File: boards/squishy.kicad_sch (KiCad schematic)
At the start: 56 parts, among them J1 USB_B_Micro, J2 Conn_02x26_Top_Bottom, J3 Conn_01x04, J4 Conn_02x05_Odd_Even, Q1 Q_PMOS_DGS, U12 SP3400-02UTG, U14 USB3318, U19 ICE40HX8K-BG121, U26 W25N01GVZEIG, X1 16MHz, X2 48MHz

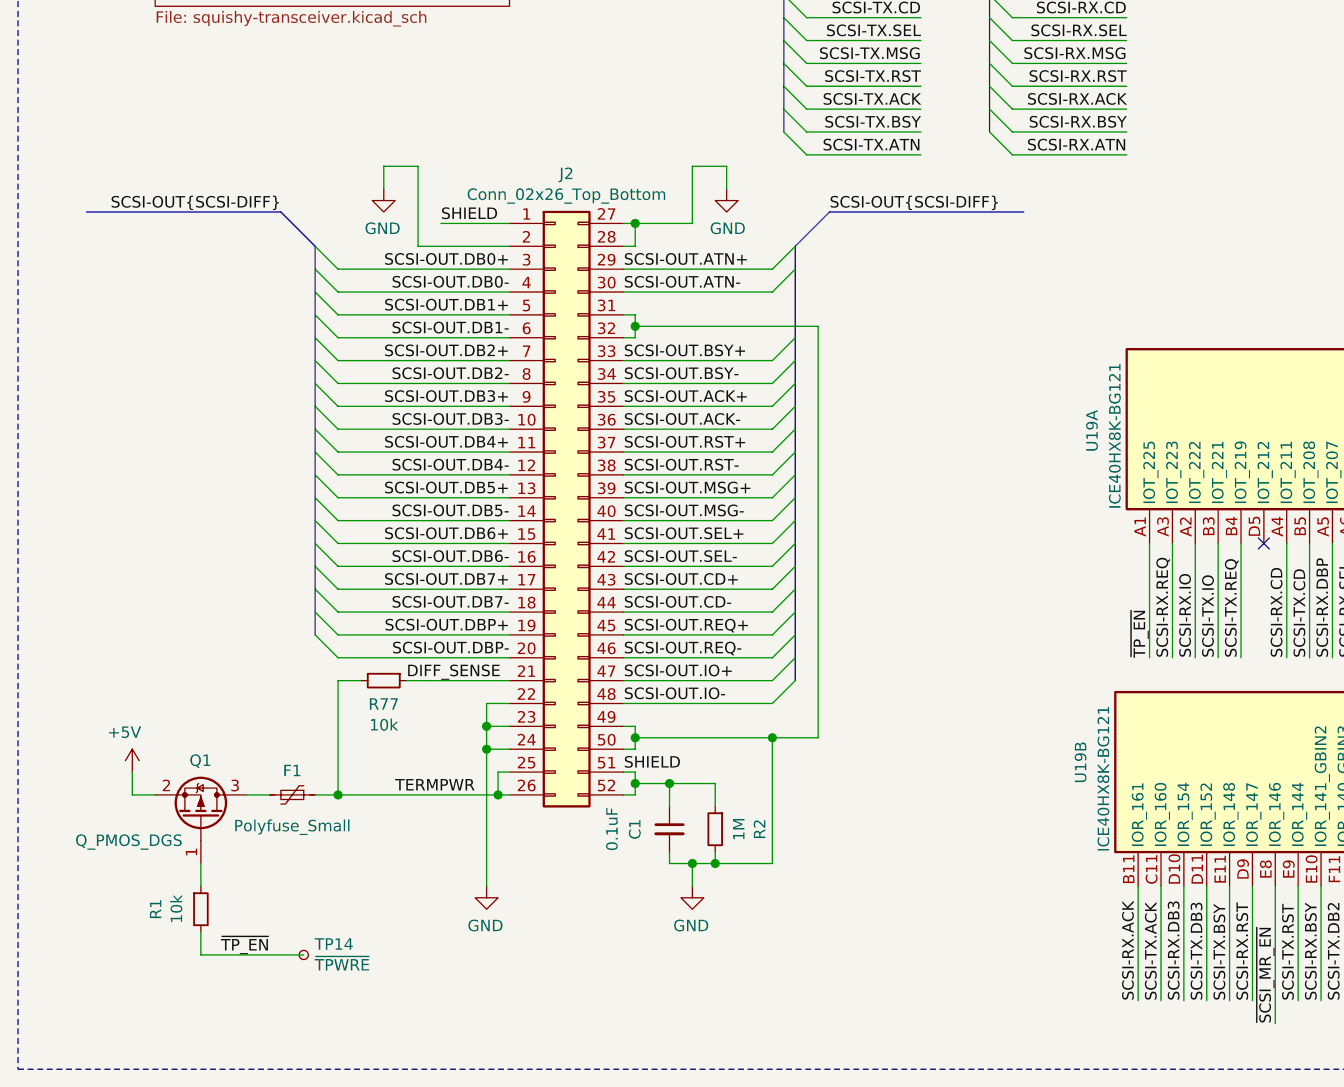
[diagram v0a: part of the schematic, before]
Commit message: hardware: found an error with how the SCSI connector was laid out, fixed that, oh no, my poor pcb
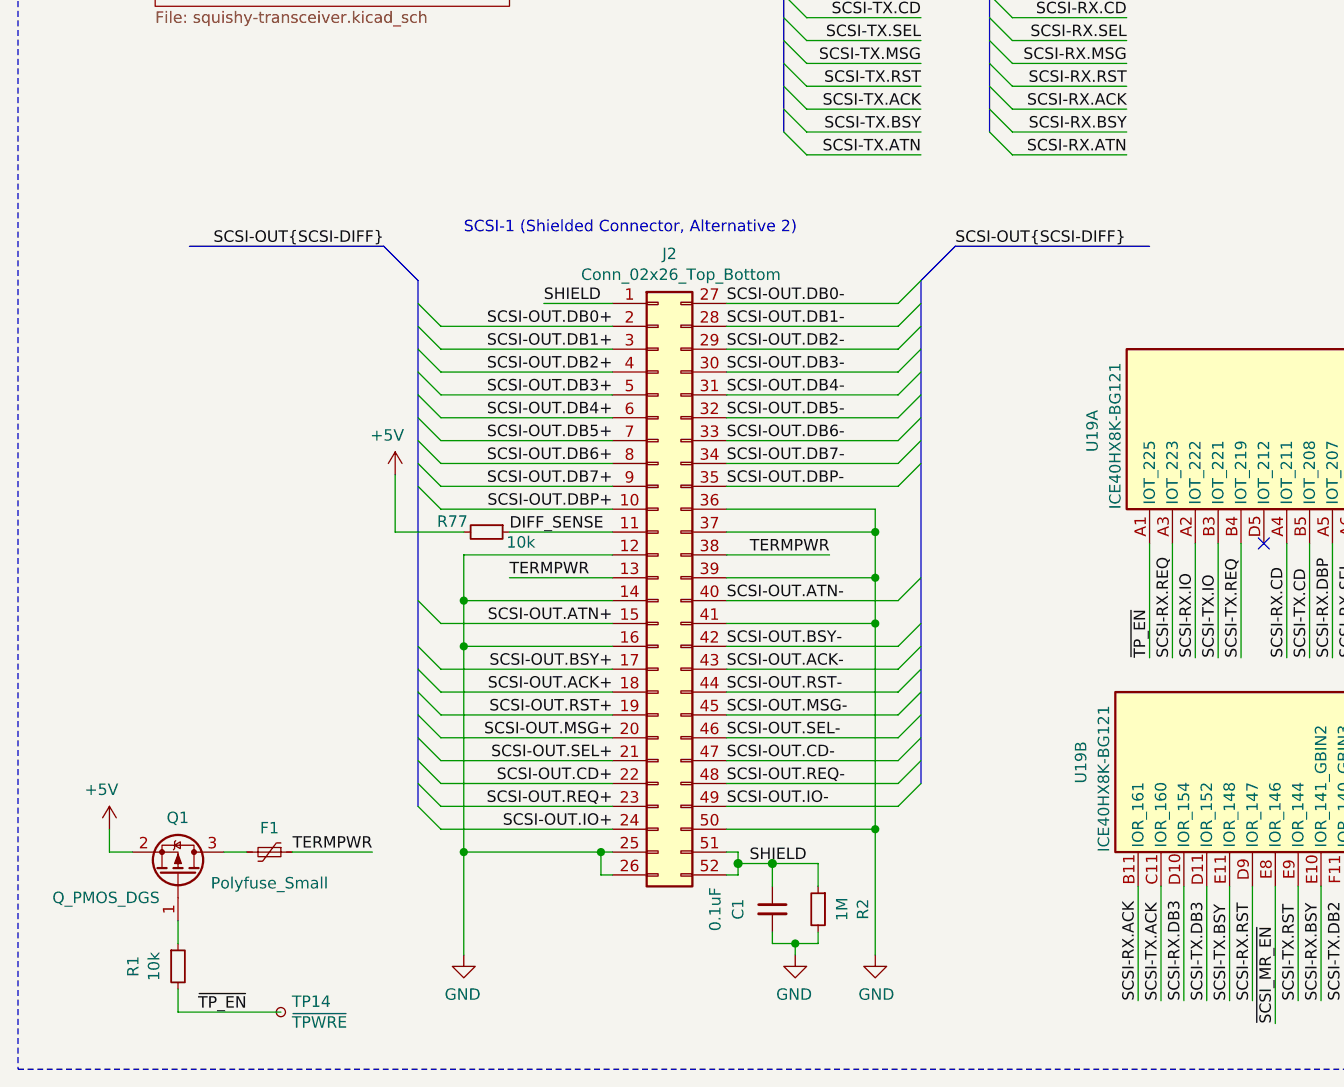
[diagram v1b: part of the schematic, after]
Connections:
- net +5V: now also R77.2
- net DIFF_SENSE: now also J2.11 (Pin_11); no longer J2.21 (Pin_21)
- net GND: now also J2.12 (Pin_12), J2.14 (Pin_14), J2.16 (Pin_16), J2.25 (Pin_25), J2.26 (Pin_26), J2.36 (Pin_36), J2.37 (Pin_37), J2.39 (Pin_39), J2.41 (Pin_41); no longer J2.2 (Pin_2), J2.22 (Pin_22), J2.23 (Pin_23), J2.24 (Pin_24), J2.27 (Pin_27), J2.28 (Pin_28), J2.31 (Pin_31), J2.32 (Pin_32), J2.49 (Pin_49)
- net SCSI-OUT.ACK+: now also J2.18 (Pin_18); no longer J2.35 (Pin_35)
- net SCSI-OUT.ACK-: now also J2.43 (Pin_43); no longer J2.36 (Pin_36)
- net SCSI-OUT.ATN+: now also J2.15 (Pin_15); no longer J2.29 (Pin_29)
- net SCSI-OUT.ATN-: now also J2.40 (Pin_40); no longer J2.30 (Pin_30)
- net SCSI-OUT.BSY+: now also J2.17 (Pin_17); no longer J2.33 (Pin_33)
- net SCSI-OUT.BSY-: now also J2.42 (Pin_42); no longer J2.34 (Pin_34)
- net SCSI-OUT.CD+: now also J2.22 (Pin_22); no longer J2.43 (Pin_43)
- net SCSI-OUT.CD-: now also J2.47 (Pin_47); no longer J2.44 (Pin_44)
- net SCSI-OUT.DB0+: now also J2.2 (Pin_2); no longer J2.3 (Pin_3)
- net SCSI-OUT.DB0-: now also J2.27 (Pin_27); no longer J2.4 (Pin_4)
- net SCSI-OUT.DB1+: now also J2.3 (Pin_3); no longer J2.5 (Pin_5)
- net SCSI-OUT.DB1-: now also J2.28 (Pin_28); no longer J2.6 (Pin_6)
- net SCSI-OUT.DB2+: now also J2.4 (Pin_4); no longer J2.7 (Pin_7)
- net SCSI-OUT.DB2-: now also J2.29 (Pin_29); no longer J2.8 (Pin_8)
- net SCSI-OUT.DB3+: now also J2.5 (Pin_5); no longer J2.9 (Pin_9)
- net SCSI-OUT.DB3-: now also J2.30 (Pin_30); no longer J2.10 (Pin_10)
- net SCSI-OUT.DB4+: now also J2.6 (Pin_6); no longer J2.11 (Pin_11)
- net SCSI-OUT.DB4-: now also J2.31 (Pin_31); no longer J2.12 (Pin_12)
- net SCSI-OUT.DB5+: now also J2.7 (Pin_7); no longer J2.13 (Pin_13)
- net SCSI-OUT.DB5-: now also J2.32 (Pin_32); no longer J2.14 (Pin_14)
- net SCSI-OUT.DB6+: now also J2.8 (Pin_8); no longer J2.15 (Pin_15)
- net SCSI-OUT.DB6-: now also J2.33 (Pin_33); no longer J2.16 (Pin_16)
- net SCSI-OUT.DB7+: now also J2.9 (Pin_9); no longer J2.17 (Pin_17)
- net SCSI-OUT.DB7-: now also J2.34 (Pin_34); no longer J2.18 (Pin_18)
- net SCSI-OUT.DBP+: now also J2.10 (Pin_10); no longer J2.19 (Pin_19)
- net SCSI-OUT.DBP-: now also J2.35 (Pin_35); no longer J2.20 (Pin_20)
- net SCSI-OUT.IO+: now also J2.24 (Pin_24); no longer J2.47 (Pin_47)
- net SCSI-OUT.IO-: now also J2.49 (Pin_49); no longer J2.48 (Pin_48)
- net SCSI-OUT.MSG+: now also J2.20 (Pin_20); no longer J2.39 (Pin_39)
- net SCSI-OUT.MSG-: now also J2.45 (Pin_45); no longer J2.40 (Pin_40)
- net SCSI-OUT.REQ+: now also J2.23 (Pin_23); no longer J2.45 (Pin_45)
- net SCSI-OUT.REQ-: now also J2.48 (Pin_48); no longer J2.46 (Pin_46)
- net SCSI-OUT.RST+: now also J2.19 (Pin_19); no longer J2.37 (Pin_37)
- net SCSI-OUT.RST-: now also J2.44 (Pin_44); no longer J2.38 (Pin_38)
- net SCSI-OUT.SEL+: now also J2.21 (Pin_21); no longer J2.41 (Pin_41)
- net SCSI-OUT.SEL-: now also J2.46 (Pin_46); no longer J2.42 (Pin_42)
- net TERMPWR: now also J2.13 (Pin_13), J2.38 (Pin_38); no longer J2.25 (Pin_25), J2.26 (Pin_26), R77.2
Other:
- note added: "SCSI-1 (Shielded Connector, Alternative 2)"
- moved on the sheet: C1, F1, J2, Q1, R1, R2, R77, TP14

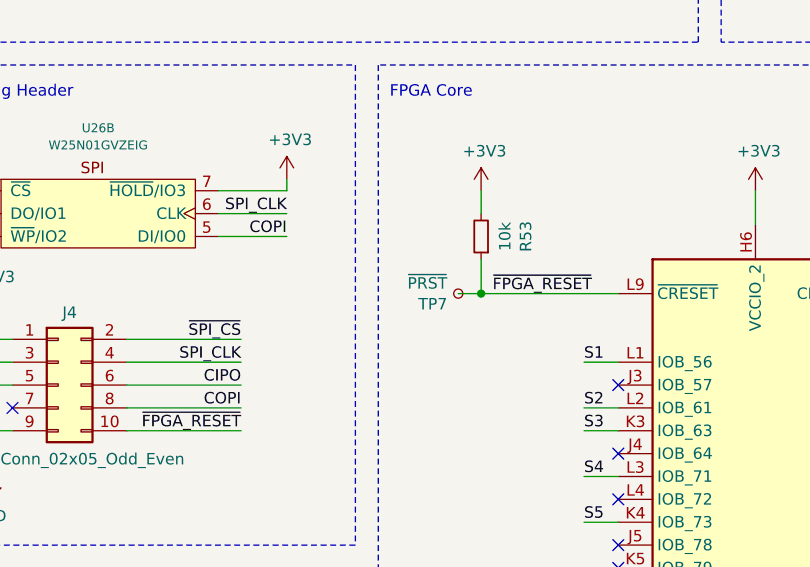
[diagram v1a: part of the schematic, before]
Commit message: hardware: ensured all of the parts had a mpn and mfr
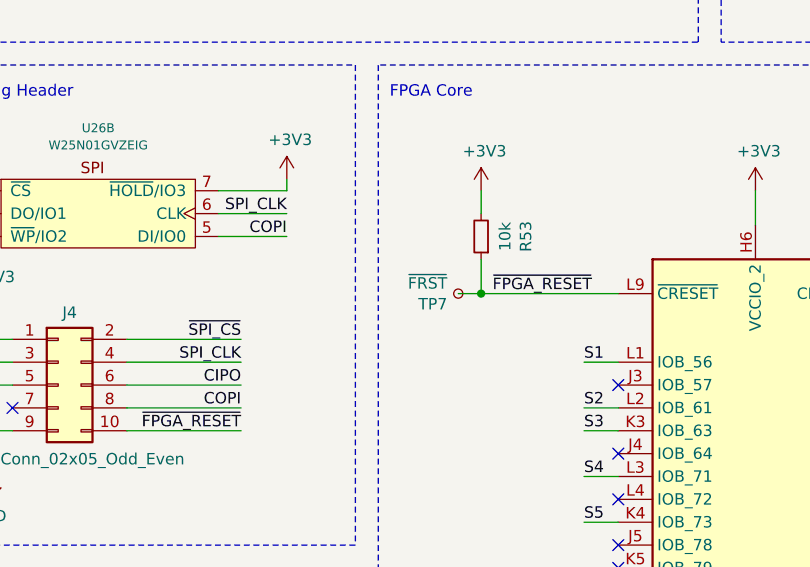
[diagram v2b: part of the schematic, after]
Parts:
- C30, C48: MFR KEMET -> Murata Electronics; MPN (none) -> GRJ21BR61E106KE01K
- C60: MFR (none) -> Taiyo Yuden; MPN (none) -> UMK107BJ105KA-T
- R57, R62: MFR (none) -> TE Connectivity Passive Product; MPN (none) -> CRG0603F100R
- R72: MFR (none) -> Vishay Dale; MPN (none) -> CRCW06038K06FKEAC
- TP10, TP11, TP12, TP13, TP14, TP6, TP8, TP9: MFR (none) -> N/A; MPN (none) -> N/A
- TP7: value ~{PRST} -> ~{FRST}; MFR (none) -> N/A; MPN (none) -> N/A
- U19: MFR Lattice Semicondutors -> Lattice Semiconductors
- U19: MFR Lattice Semiconducrtors -> Lattice Semiconductors
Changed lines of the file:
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@@
       (effects (font (size 1.27 1.27)) hide)
     )
+    (property "MFR" "N/A" (id 4) (at 30.48 121.92 0)
+      (effects (font (size 1.27 1.27)) hide)
+    )
+    (property "MPN" "N/A" (id 5) (at 30.48 121.92 0)
+      (effects (font (size 1.27 1.27)) hide)
+    )
     (pin "1")
   )
@@
       (effects (font (size 1.27 1.27)) hide)
     )
+    (property "MFR" "N/A" (id 4) (at 43.18 276.86 0)
+      (effects (font (size 1.27 1.27)) hide)
+    )
+    (property "MPN" "N/A" (id 5) (at 43.18 276.86 0)
+      (effects (font (size 1.27 1.27)) hide)
+    )
     (pin "1")
   )
@@
       (effects (font (size 1.27 1.27)) hide)
     )
+    (property "MFR" "N/A" (id 4) (at 208.28 133.35 0)
+      (effects (font (size 1.27 1.27)) hide)
+    )
+    (property "MPN" "N/A" (id 5) (at 208.28 133.35 0)
+      (effects (font (size 1.27 1.27)) hide)
+    )
     (pin "1")
   )
@@
       (effects (font (size 1.27 1.27)) hide)
     )
+    (property "MFR" "N/A" (id 4) (at 208.28 138.43 0)
+      (effects (font (size 1.27 1.27)) hide)
+    )
+    (property "MPN" "N/A" (id 5) (at 208.28 138.43 0)
+      (effects (font (size 1.27 1.27)) hide)
+    )
     (pin "1")
   )
@@
       (effects (font (size 1.27 1.27)) hide)
     )
+    (property "MFR" "N/A" (id 4) (at 208.28 143.51 0)
+      (effects (font (size 1.27 1.27)) hide)
+    )
+    (property "MPN" "N/A" (id 5) (at 208.28 143.51 0)
+      (effects (font (size 1.27 1.27)) hide)
+    )
     (pin "1")
   )
@@
       (effects (font (size 1.27 1.27)) hide)
     )
+    (property "MFR" "N/A" (id 4) (at 208.28 148.59 0)
+      (effects (font (size 1.27 1.27)) hide)
+    )
+    (property "MPN" "N/A" (id 5) (at 208.28 148.59 0)
+      (effects (font (size 1.27 1.27)) hide)
+    )
     (pin "1")
   )
@@
       (effects (font (size 1.27 1.27)) hide)
     )
+    (property "MFR" "N/A" (id 4) (at 208.28 153.67 0)
+      (effects (font (size 1.27 1.27)) hide)
+    )
+    (property "MPN" "N/A" (id 5) (at 208.28 153.67 0)
+      (effects (font (size 1.27 1.27)) hide)
+    )
     (pin "1")
   )
@@
       (effects (font (size 1.27 1.27)) hide)
     )
+    (property "MFR" "N/A" (id 4) (at 208.28 158.75 0)
+      (effects (font (size 1.27 1.27)) hide)
+    )
+    (property "MPN" "N/A" (id 5) (at 208.28 158.75 0)
+      (effects (font (size 1.27 1.27)) hide)
+    )
     (pin "1")
   )
@@
       (effects (font (size 1.27 1.27)) (justify left))
     )
-    (property "Value" "~{PRST}" (id 1) (at 227.3808 96.647 0)
+    (property "Value" "~{FRST}" (id 1) (at 227.3808 96.647 0)
       (effects (font (size 1.27 1.27)) (justify left))
     )
@@
       (effects (font (size 1.27 1.27)) hide)
     )
+    (property "MFR" "N/A" (id 4) (at 228.6 97.79 0)
+      (effects (font (size 1.27 1.27)) hide)
+    )
+    (property "MPN" "N/A" (id 5) (at 228.6 97.79 0)
+      (effects (font (size 1.27 1.27)) hide)
+    )
     (pin "1")
   )
@@
       (effects (font (size 1.27 1.27)) hide)
     )
-    (property "MFR" "" (id 4) (at 123.19 35.56 90)
+    (property "MFR" "Vishay Dale" (id 4) (at 123.19 35.56 90)
       (effects (font (size 1.27 1.27)) hide)
     )
-    (property "MPN" "" (id 5) (at 123.19 35.56 90)
+    (property "MPN" "CRCW06038K06FKEAC" (id 5) (at 123.19 35.56 90)
       (effects (font (size 1.27 1.27)) hide)
     )
@@
       (effects (font (size 1.27 1.27)) hide)
     )
-    (property "MFR" "" (id 4) (at 331.47 101.6 90)
+    (property "MFR" "TE Connectivity Passive Product" (id 4) (at 331.47 101.6 90)
       (effects (font (size 1.27 1.27)) hide)
     )
-    (property "MPN" "" (id 5) (at 331.47 101.6 90)
+    (property "MPN" "CRG0603F100R" (id 5) (at 331.47 101.6 90)
       (effects (font (size 1.27 1.27)) hide)
     )
@@
       (effects (font (size 1.27 1.27)) hide)
     )
-    (property "MFR" "" (id 4) (at 339.09 101.6 90)
+    (property "MFR" "TE Connectivity Passive Product" (id 4) (at 339.09 101.6 90)
       (effects (font (size 1.27 1.27)) hide)
     )
-    (property "MPN" "" (id 5) (at 339.09 101.6 90)
+    (property "MPN" "CRG0603F100R" (id 5) (at 339.09 101.6 90)
       (effects (font (size 1.27 1.27)) hide)
     )
@@
       (effects (font (size 1.27 1.27)) hide)
     )
-    (property "MFR" "" (id 4) (at 31.75 44.45 90)
+    (property "MFR" "Taiyo Yuden" (id 4) (at 31.75 44.45 90)
       (effects (font (size 1.27 1.27)) hide)
     )
-    (property "MPN" "" (id 5) (at 31.75 44.45 90)
+    (property "MPN" "UMK107BJ105KA-T" (id 5) (at 31.75 44.45 90)
       (effects (font (size 1.27 1.27)) hide)
     )
@@
       (effects (font (size 1.27 1.27)) hide)
     )
-    (property "MFR" "KEMET" (id 4) (at 326.39 111.76 90)
+    (property "MFR" "Murata Electronics" (id 4) (at 326.39 111.76 90)
       (effects (font (size 1.27 1.27)) hide)
     )
-    (property "MPN" "" (id 5) (at 326.39 111.76 90)
+    (property "MPN" "GRJ21BR61E106KE01K" (id 5) (at 326.39 111.76 90)
       (effects (font (size 1.27 1.27)) hide)
     )
@@
       (effects (font (size 1.27 1.27)) hide)
     )
-    (property "MFR" "KEMET" (id 4) (at 326.39 121.92 90)
+    (property "MFR" "Murata Electronics" (id 4) (at 326.39 121.92 90)
       (effects (font (size 1.27 1.27)) hide)
     )
-    (property "MPN" "" (id 5) (at 326.39 121.92 90)
+    (property "MPN" "GRJ21BR61E106KE01K" (id 5) (at 326.39 121.92 90)
       (effects (font (size 1.27 1.27)) hide)
     )
@@
       (effects (font (size 1.27 1.27)) hide)
     )
-    (property "MFR" "Lattice Semicondutors" (id 4) (at 168.91 250.19 0)
+    (property "MFR" "Lattice Semiconductors" (id 4) (at 168.91 250.19 0)
       (effects (font (size 1.27 1.27)) hide)
     )
@@
       (effects (font (size 1.27 1.27)) hide)
     )
-    (property "MFR" "Lattice Semiconducrtors" (id 4) (at 109.22 76.2 0)
+    (property "MFR" "Lattice Semiconductors" (id 4) (at 109.22 76.2 0)
       (effects (font (size 1.27 1.27)) hide)
     )
@@
     )
     (path "/c65a6615-4b3e-4786-acd8-db1b7e11db3e"
-      (reference "TP7") (unit 1) (value "~{PRST}") (footprint "TestPoint:TestPoint_Pad_D1.0mm")
+      (reference "TP7") (unit 1) (value "~{FRST}") (footprint "TestPoint:TestPoint_Pad_D1.0mm")
     )
     (path "/507e02d1-bc33-4641-a7ed-cead94c55d4a"
